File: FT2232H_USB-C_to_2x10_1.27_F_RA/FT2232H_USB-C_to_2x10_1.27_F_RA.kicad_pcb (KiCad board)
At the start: 4 copper layers, 39 parts, among them J1 USB_B_Micro, J2 Conn_02x10_Odd_Even, J3 Conn_02x10_Odd_Even, U1 FT2232HL, U2 93C46BT-I_OT, U3 USBLC6-2SC6, U4 MIC5504-3.3YM5, X1 DSC60xx

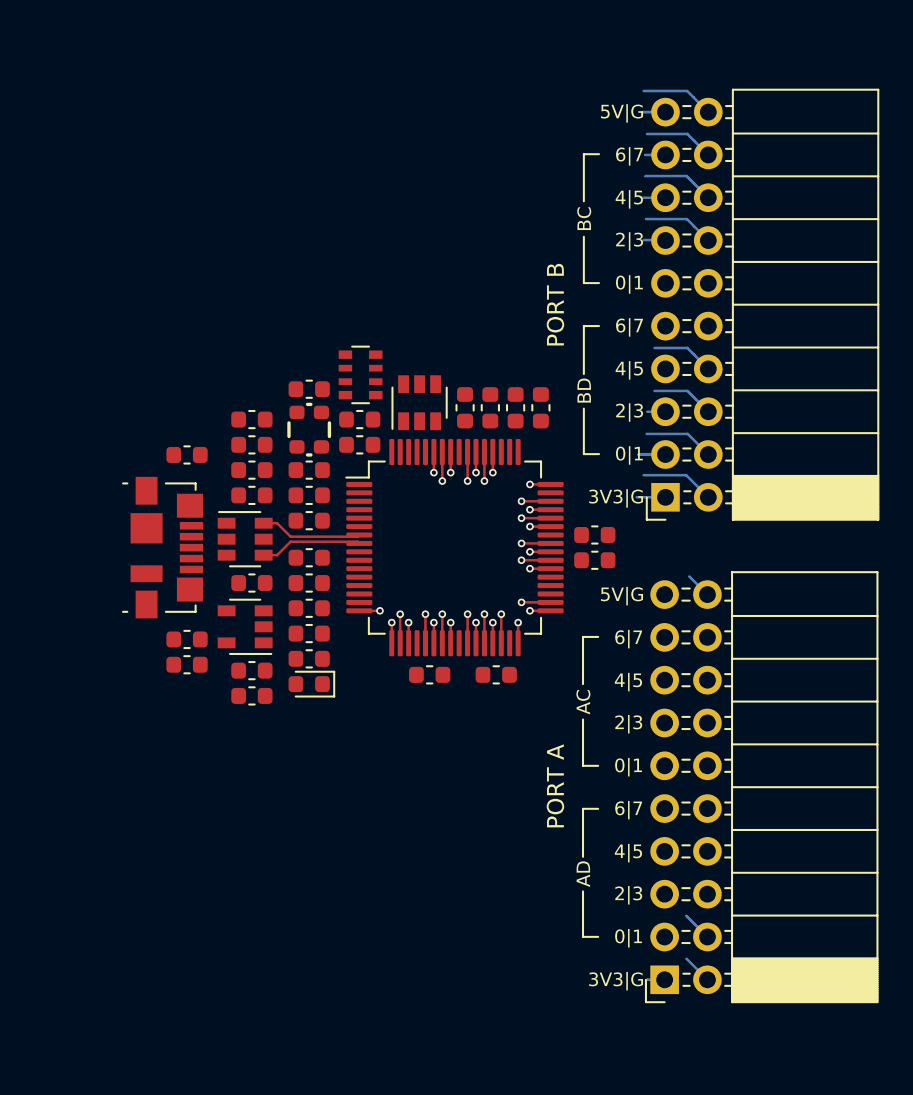
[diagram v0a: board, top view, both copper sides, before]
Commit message: Adjusting placement for FT2232_USB-C
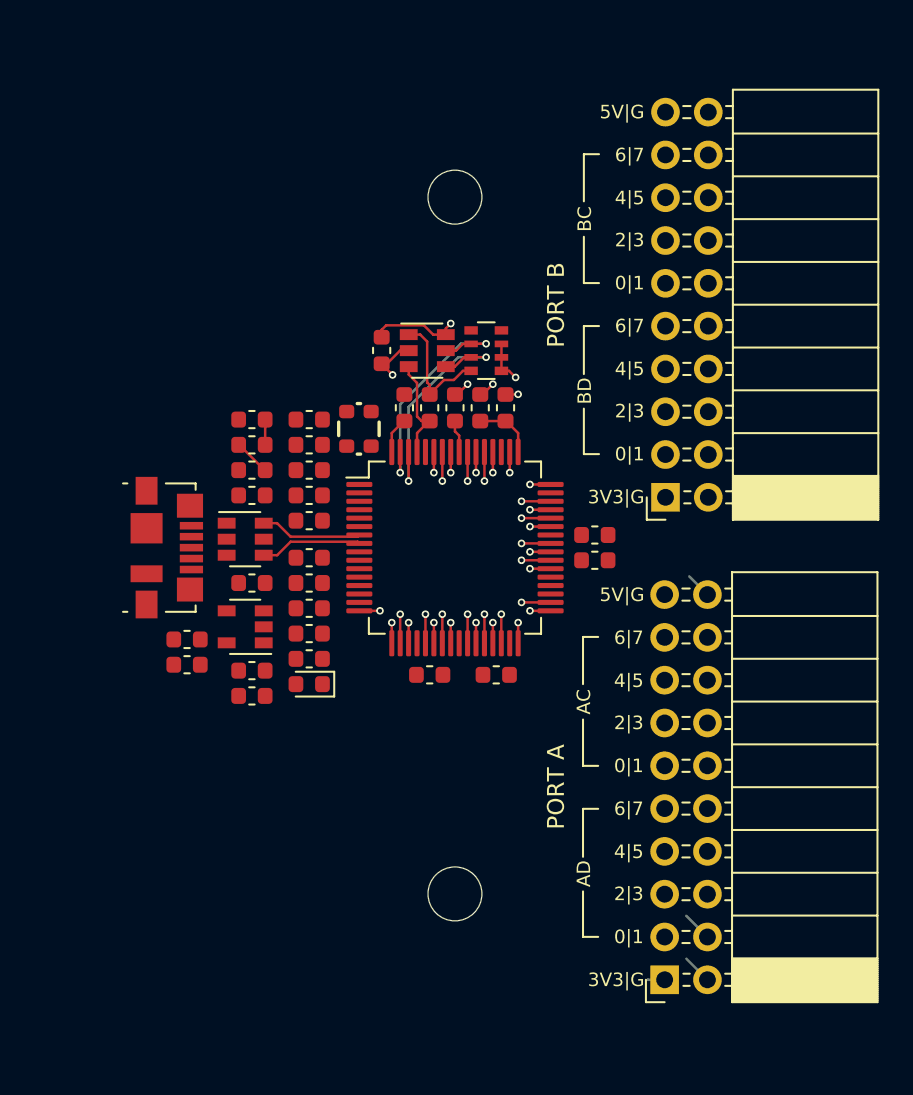
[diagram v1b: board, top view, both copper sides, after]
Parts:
- added H1: MountingHole_M3, MountingHole:MountingHole_3.2mm_M3, F.Cu at (161.0, 117.6)
- added H2: MountingHole_M3, MountingHole:MountingHole_3.2mm_M3, F.Cu at (161.0, 76.2)
- moved R3 8.23 mm to (152.3, 95.4)
- moved R4 7.60 mm to (162.9, 85.3), turned to 0 degrees
- moved C7 4.30 mm to (156.7, 85.3), turned to 270 degrees
- moved C1 3.60 mm to (162.5, 88.7)
- moved C17 3.44 mm to (158.0, 88.7), turned to 90 degrees
- moved U2 3.12 mm to (159.4, 85.3), turned to 0 degrees
- moved X1 2.95 mm to (155.3, 90.0)
- moved C12 2.10 mm to (161.0, 88.7)
- moved R5 2.10 mm to (159.5, 88.7)
- moved C8 1.80 mm to (152.3, 89.4)
- moved C13 1.50 mm to (152.3, 92.4)
- moved C14 1.50 mm to (152.3, 93.9)
- moved FB2 1.50 mm to (152.3, 90.9)
- moved C2 0.60 mm to (164.0, 88.7)
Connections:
- J2 pad 1: /AD0 -> GND
- J2 pad 10: GND -> /AD7
- J2 pad 11: P3V3 -> /AC0
- J2 pad 12: GND -> /AC1
- J2 pad 13: /AC0 -> /AC2
- J2 pad 14: /AC1 -> /AC3
- J2 pad 15: /AC2 -> /AC4
- J2 pad 16: /AC3 -> /AC5
- J2 pad 17: /AC4 -> /AC6
- J2 pad 18: /AC5 -> /AC7
- J2 pad 19: /AC6 -> GND
- J2 pad 2: /AD1 -> USB_5V
- J2 pad 20: /AC7 -> P3V3
- J2 pad 3: /AD2 -> /AD0
- J2 pad 4: /AD3 -> /AD1
- J2 pad 5: /AD4 -> /AD2
- J2 pad 6: /AD5 -> /AD3
- J2 pad 7: /AD6 -> /AD4
- J2 pad 8: /AD7 -> /AD5
- J2 pad 9: USB_5V -> /AD6
- J3 pad 1: /BD0 -> GND
- J3 pad 10: GND -> /BD7
- J3 pad 11: P3V3 -> /BC0
- J3 pad 12: GND -> /BC1
- J3 pad 13: /BC0 -> /BC2
- J3 pad 14: /BC1 -> /BC3
- J3 pad 15: /BC2 -> /BC4
- J3 pad 16: /BC3 -> /BC5
- J3 pad 17: /BC4 -> /BC6
- J3 pad 18: /BC5 -> /BC7
- J3 pad 19: /BC6 -> GND
- J3 pad 2: /BD1 -> USB_5V
- J3 pad 20: /BC7 -> P3V3
- J3 pad 3: /BD2 -> /BD0
- J3 pad 4: /BD3 -> /BD1
- J3 pad 5: /BD4 -> /BD2
- J3 pad 6: /BD5 -> /BD3
- J3 pad 7: /BD6 -> /BD4
- J3 pad 8: /BD7 -> /BD5
- J3 pad 9: USB_5V -> /BD6
- R4 pad 1: /USB_EECS -> Net-(R4-Pad1)
- R4 pad 2: /USB_EECLK -> /USB_EECS
- R4 pad 3: /USB_EEDO -> /USB_EECLK
- R4 pad 4: Net-(R4-Pad4) -> /USB_EEDO
- R4 pad 5: Net-(R4-Pad5) -> P3V3
- R4 pad 8: P3V3 -> Net-(R4-Pad8)
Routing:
- net /USB_EECLK: track 0.00 -> 14.6 mm, vias 0 -> 2
- net /USB_EECS: track 0.00 -> 14.4 mm, vias 0 -> 2
- net P3V3: track 0.00 -> 12.7 mm, vias 0 -> 3
- net GND: track 0.00 -> 8.13 mm, vias 0 -> 4
- net /USB_EEDO: track 0.00 -> 7.51 mm
- net /USB_EEDATA: track 0.00 -> 6.19 mm
- net P1V8: track 0.00 -> 5.84 mm
- net /BD1: track 6.10 -> 1.73 mm
- net /BC7: track 5.58 -> 1.23 mm
- net /BC3: track 5.49 -> 1.23 mm
- net /BC1: track 5.44 -> 1.23 mm
- net /BD3: track 5.89 -> 1.73 mm
- net /BC5: track 5.37 -> 1.23 mm
- net USB_5V: track 0.00 -> 3.96 mm
- net /BD5: track 5.43 -> 1.73 mm
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
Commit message: Add Nelgau-Logo to FT2232H_USB-C
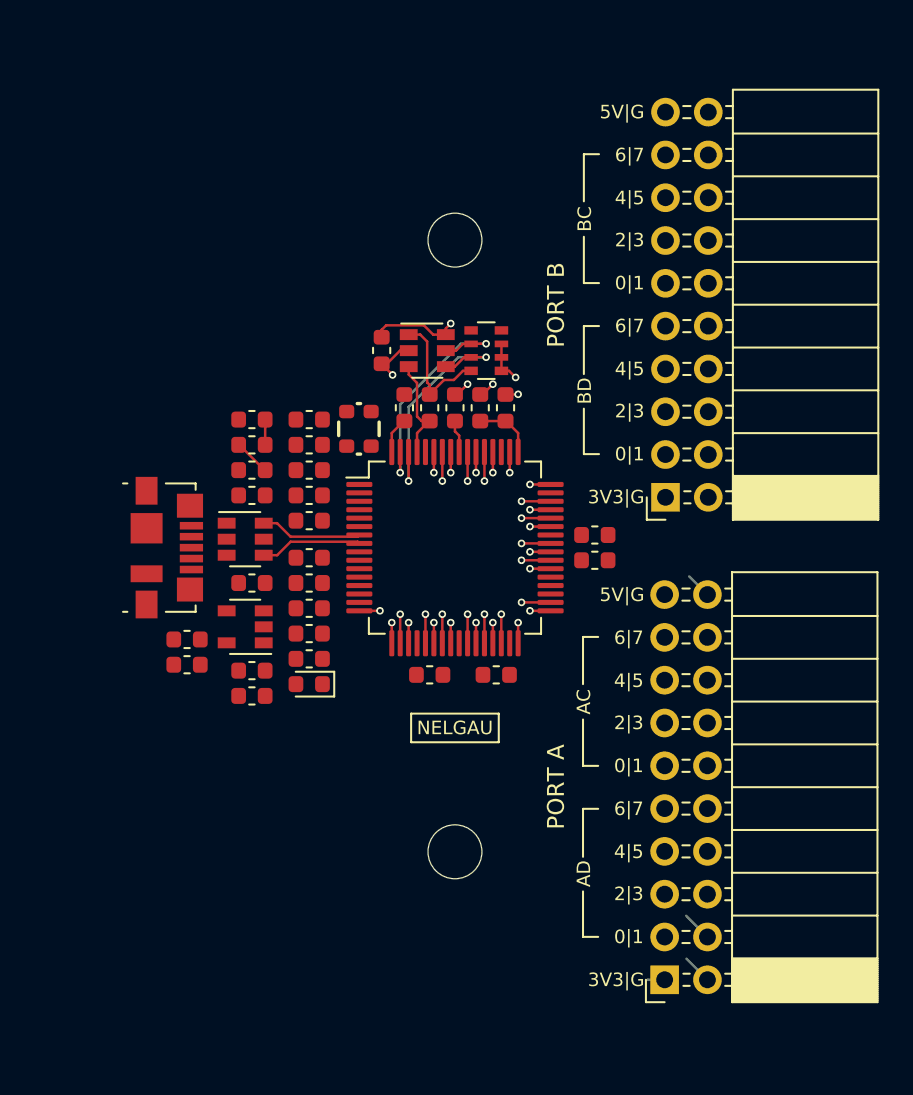
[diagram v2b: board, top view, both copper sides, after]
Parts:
- added SYM1: Nelgau-Logo, ng_symbol:Nelgau-Logo_5.2x1.7mm_SilkScreen, F.Cu at (161.0, 107.7)
- moved H2 2.55 mm to (161.0, 78.8)
- moved H1 2.50 mm to (161.0, 115.1)
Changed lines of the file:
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@@
     (tracks 166)
     (zones 0)
-    (modules 41)
+    (modules 42)
     (nets 60)
   )
@@
     (add_net /xUSB_D-)
   )
+  (module ng_symbol:Nelgau-Logo_5.2x1.7mm_SilkScreen (layer F.Cu)
+    (at 161 107.728)
+    (descr "Nelgau Logo")
+    (tags "Logo Nelgau")
+    (attr virtual)
+    (fp_text reference SYM1 (at 0 2) (layer F.SilkS) hide
+      (effects (font (size 1 1) (thickness 0.15)))
+    )
+    (fp_text value Nelgau-Logo (at 0 3.5) (layer F.Fab) hide
+      (effects (font (size 1 1) (thickness 0.15)))
+    )
+    (fp_line (start -2.8 1.1) (end -2.8 -1.1) (layer F.CrtYd) (width 0.05))
+    (fp_line (start 2.8 1.1) (end -2.8 1.1) (layer F.CrtYd) (width 0.05))
+    (fp_line (start 2.8 -1.1) (end 2.8 1.1) (layer F.CrtYd) (width 0.05))
+    (fp_line (start -2.8 -1.1) (end 2.8 -1.1) (layer F.CrtYd) (width 0.05))
+    (fp_text user NELGAU (at 0 0) (layer F.SilkS)
+      (effects (font (size 0.8 0.8) (thickness 0.15)))
+    )
+    (fp_line (start 2.6 -0.85) (end 2.6 0.85) (layer F.SilkS) (width 0.12))
+    (fp_line (start -2.6 -0.85) (end -2.6 0.85) (layer F.SilkS) (width 0.12))
+    (fp_line (start -2.6 0.85) (end 2.6 0.85) (layer F.SilkS) (width 0.12))
+    (fp_line (start -2.6 -0.85) (end 2.6 -0.85) (layer F.SilkS) (width 0.12))
+  )
   (module MountingHole:MountingHole_3.2mm_M3 (layer F.Cu)
-    (at 161 76.228)
+    (at 161 78.778)
     (descr "Mounting Hole 3.2mm, no annular, M3")
     (tags "mounting hole 3.2mm no annular m3")
@@
   )
   (module MountingHole:MountingHole_3.2mm_M3 (layer F.Cu)
-    (at 161 117.578)
+    (at 161 115.078)
     (descr "Mounting Hole 3.2mm, no annular, M3")
     (tags "mounting hole 3.2mm no annular m3")
@@
   (segment (start 156.65 86.128) (end 157.3 86.778) (width 0.15) (layer F.Cu) (net 1))
   (segment (start 156.65 86.1155) (end 156.65 86.128) (width 0.15) (layer F.Cu) (net 1))
+  (segment (start 172.444 122.674) (end 172.44 122.678) (width 0.15) (layer B.Cu) (net 1))
+  (segment (start 173.444 122.674) (end 172.444 122.674) (width 0.15) (layer B.Cu) (net 1))
   (segment (start 162.975 89.5155) (end 164 89.5155) (width 0.15) (layer F.Cu) (net 2))
   (segment (start 162.5 89.5155) (end 162.975 89.5155) (width 0.15) (layer F.Cu) (net 2))
@@
   (segment (start 148.2 90.928) (end 149.7 92.428) (width 0.15) (layer F.Cu) (net 4))
   (segment (start 148.1625 90.928) (end 148.2 90.928) (width 0.15) (layer F.Cu) (net 4))
+  (segment (start 175.984 122.674) (end 174.738 121.428) (width 0.15) (layer B.Cu) (net 4))
   (segment (start 161.25 90.378) (end 161.25 91.353) (width 0.15) (layer F.Cu) (net 6))
   (segment (start 161 90.128) (end 161.25 90.378) (width 0.15) (layer F.Cu) (net 6))
@@
   (via (at 164.25 92.578) (size 0.45) (drill 0.25) (layers F.Cu B.Cu) (net 6))
   (segment (start 164.25 91.353) (end 164.25 92.578) (width 0.15) (layer F.Cu) (net 6))
+  (segment (start 175.984 99.814) (end 174.908999 98.738999) (width 0.15) (layer B.Cu) (net 6))
   (via (at 164.95 100.278) (size 0.45) (drill 0.25) (layers F.Cu B.Cu) (net 13))
   (segment (start 166.675 100.278) (end 164.95 100.278) (width 0.15) (layer F.Cu) (net 13))
-  (segment (start 175.984 99.814) (end 174.908999 98.738999) (width 0.15) (layer B.Cu) (net 6))
   (via (at 165.45 100.778) (size 0.45) (drill 0.25) (layers F.Cu B.Cu) (net 14))
   (segment (start 166.675 100.778) (end 165.45 100.778) (width 0.15) (layer F.Cu) (net 14))
@@
   (via (at 158.25 101.478) (size 0.45) (drill 0.25) (layers F.Cu B.Cu) (net 25))
   (segment (start 158.25 102.703) (end 158.25 101.478) (width 0.15) (layer F.Cu) (net 25))
-  (segment (start 175.984 120.134) (end 174.728 118.878) (width 0.15) (layer B.Cu) (net 27))
   (via (at 157.75 100.978) (size 0.45) (drill 0.25) (layers F.Cu B.Cu) (net 26))
   (segment (start 157.75 102.703) (end 157.75 100.978) (width 0.15) (layer F.Cu) (net 26))
+  (segment (start 175.984 120.134) (end 174.728 118.878) (width 0.15) (layer B.Cu) (net 27))
   (via (at 157.25 101.478) (size 0.45) (drill 0.25) (layers F.Cu B.Cu) (net 27))
   (segment (start 157.25 102.703) (end 157.25 101.478) (width 0.15) (layer F.Cu) (net 27))
-  (segment (start 175.984 122.674) (end 174.738 121.428) (width 0.15) (layer B.Cu) (net 4))
   (via (at 156.55 100.778) (size 0.45) (drill 0.25) (layers F.Cu B.Cu) (net 28))
   (segment (start 155.325 100.778) (end 156.55 100.778) (width 0.15) (layer F.Cu) (net 28))
-  (segment (start 172.444 122.674) (end 172.44 122.678) (width 0.15) (layer B.Cu) (net 1))
-  (segment (start 173.444 122.674) (end 172.444 122.674) (width 0.15) (layer B.Cu) (net 1))
   (via (at 159.75 92.578) (size 0.45) (drill 0.25) (layers F.Cu B.Cu) (net 29))
   (segment (start 159.75 91.353) (end 159.75 92.578) (width 0.15) (layer F.Cu) (net 29))

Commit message: Routed all dense nets near FT2232H
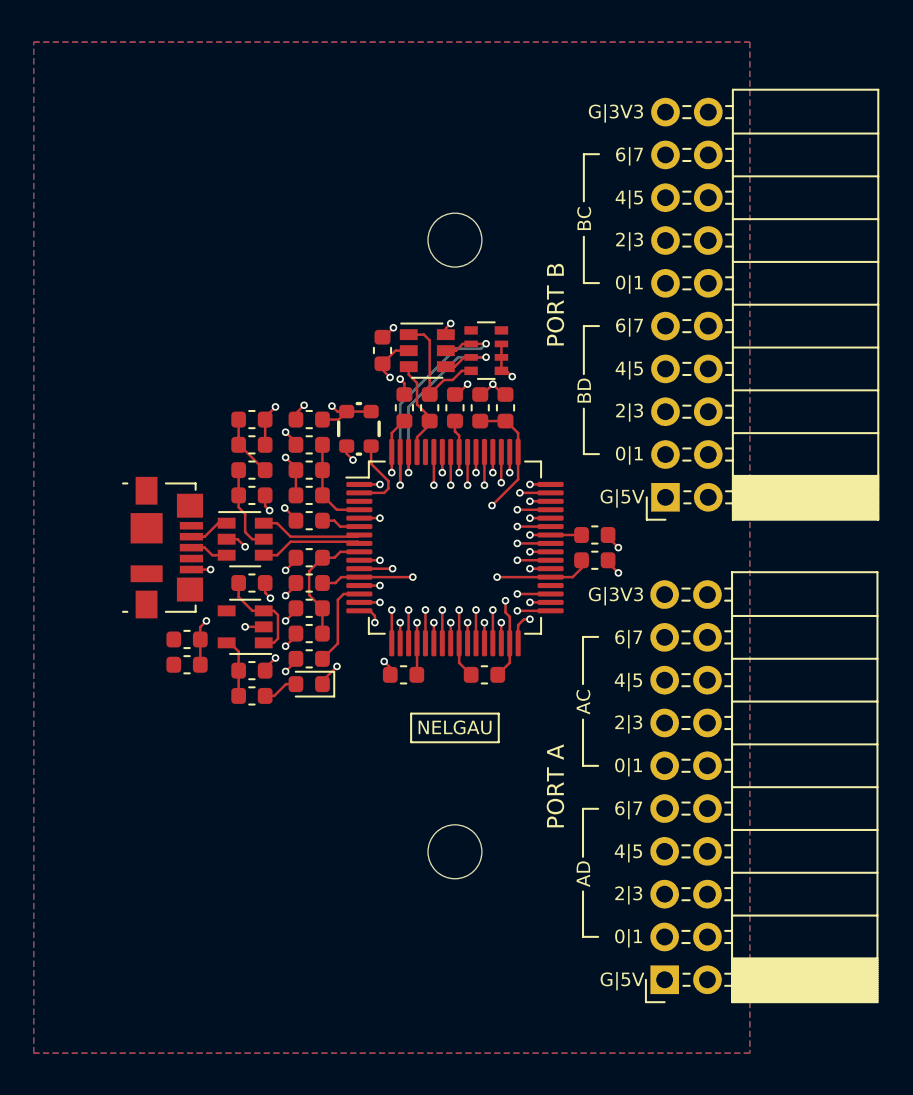
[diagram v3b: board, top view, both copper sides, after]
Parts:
- moved C9 1.55 mm to (157.9, 104.6), turned to 180 degrees
- moved C10 0.70 mm to (162.8, 104.6)
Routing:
- net GND: track 8.13 -> 49.6 mm, vias 4 -> 33
- net P3V3: track 12.7 -> 30.3 mm, vias 3 -> 12
- net P1V8: track 5.84 -> 22.1 mm, vias 0 -> 4
- net VPLL: track 0.00 -> 7.48 mm
- net USB_5V: track 3.96 -> 9.66 mm
- net VPHY: track 0.00 -> 5.54 mm
- net Net-(R2-Pad1): track 0.00 -> 5.30 mm
- net /USB_VBUS: track 0.00 -> 5.11 mm
- net /USB_OSC: track 0.00 -> 4.78 mm
- net /xUSB_D-: track 0.00 -> 2.42 mm
- net Net-(R3-Pad1): track 0.00 -> 2.33 mm
- net /xUSB_D+: track 0.00 -> 2.28 mm
- net Net-(D1-Pad2): track 0.00 -> 2.11 mm
- net /USB_EECS: track 14.4 -> 15.9 mm
- net /AD1: track 3.00 -> 1.98 mm
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- added copper zone on B.Cu, net GND
- added copper zone on F.Cu, net GND
- added copper zone on In1(GND).Cu, net GND
- added copper zone on In2(PWR).Cu, net P1V8
- added copper zone on In2(PWR).Cu, net P3V3
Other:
- board text added: "G|3V3"
- board text added: "G|5V"
- board text removed: "3V3|G"
- board text removed: "5V|G"

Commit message: Add tentative board edge and trim pin socket footprints
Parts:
- J2, J3: footprint Connector_PinSocket_2.54mm:PinSocket_2x10_P2.54mm_Horizontal -> local_conn:PinSocket_2x10_P2.54mm_Horizontal
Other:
- board outline added: 37.2 x 57 mm

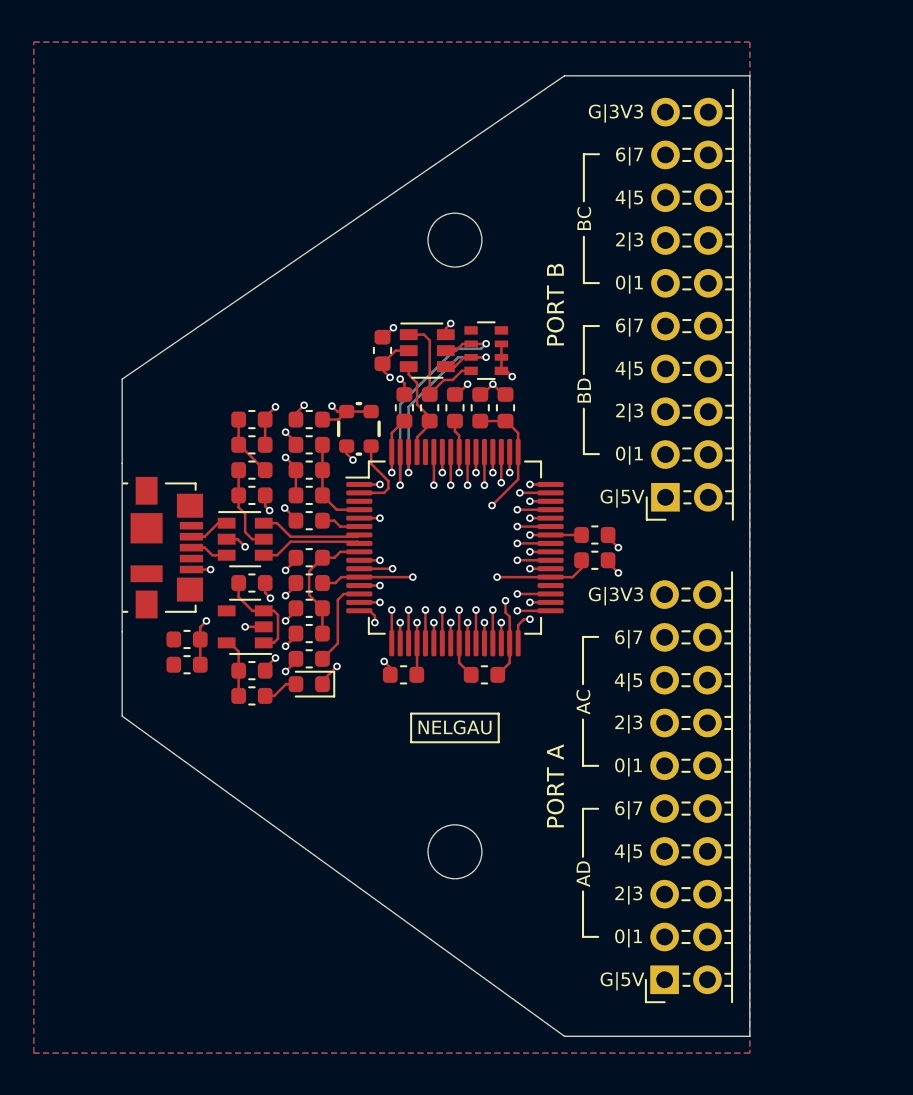
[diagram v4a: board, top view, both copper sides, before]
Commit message: Set final pin socket clearance
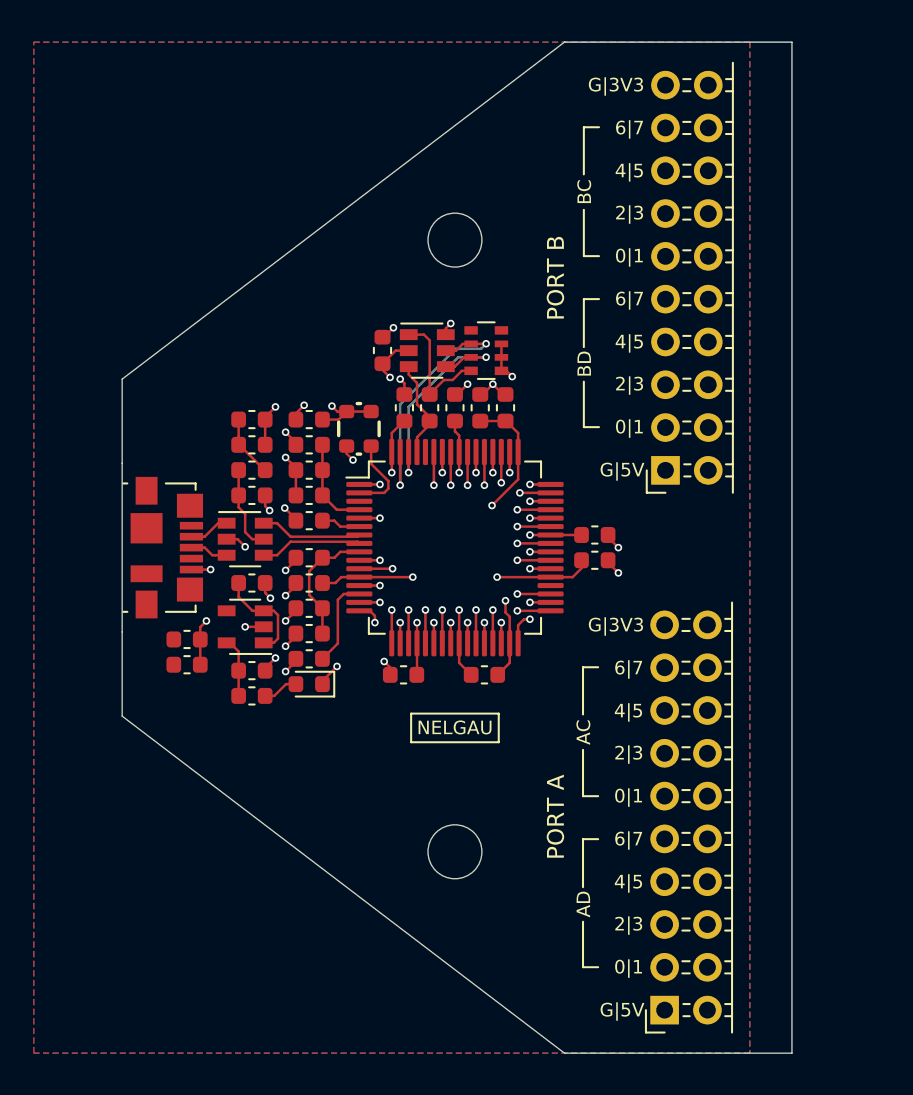
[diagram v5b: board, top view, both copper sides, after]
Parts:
- moved J2 1.80 mm to (173.4, 124.5)
- moved J3 1.60 mm to (173.5, 92.4)
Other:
- board size 37.2 x 57 mm -> 39.8 x 60 mm
